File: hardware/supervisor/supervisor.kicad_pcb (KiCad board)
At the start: 2 copper layers, 65 x 56.5 mm, 42 parts, among them IC1 LM2596-3.3, IC10 SIM900, IC2 ULN2003A, IC3 MAX1161?, IC4 ACS723LLCTR-10AU-T, IC5 ACS723LLCTR-10AU-T, IC6 ACS723LLCTR-10AU-T, IC7 ACS723LLCTR-10AU-T, IC8 NLSX4373, IC9 NLSX4373, K1 RELAY, K2 RELAY, P1 RASPI-CONNECT, P2 POWER, P3 RELAY CONNECTOR, P4 TO STRINGS, P5 TO GAK, SW1 SW_PUSH, SW2 SW_PUSH, U1 RF_CONN, U2 SIM_HOLDER

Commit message: master pcb work
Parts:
- added P6: string2, Pin_Headers:Pin_Header_Straight_2x01, F.Cu at (152.4, 153.7)
- added P7: string3, Pin_Headers:Pin_Header_Straight_2x01, F.Cu at (158.8, 153.7)
- C8, IC1: moved to B.Cu
- P4: value TO STRINGS -> string0; footprint Pin_Headers:Pin_Header_Straight_1x04 -> Pin_Headers:Pin_Header_Straight_2x01
- P5: value TO GAK -> string1; footprint Pin_Headers:Pin_Header_Straight_1x04 -> Pin_Headers:Pin_Header_Straight_2x01
- moved IC8 19.1 mm to (134.6, 123.2)
- moved IC9 17.7 mm to (142.2, 123.8)
- moved IC4 13.0 mm to (141.0, 147.3)
- moved P4 12.8 mm to (139.7, 153.7), turned to 0 degrees
- moved P5 10.2 mm to (146.1, 153.7), turned to 0 degrees
- moved IC3 9.38 mm to (150.5, 137.8)
- moved IC5 6.84 mm to (147.3, 147.3)
- moved IC6 6.84 mm to (153.7, 147.3)
- moved D1 2.84 mm to (158.8, 125.7)
- moved L1 2.54 mm to (149.9, 125.7)
- moved IC7 2.54 mm to (160.0, 147.3)
- moved IC1 1.27 mm to (149.9, 115.6)
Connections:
- P4 pad 1: string_in3 -> string_out0
- P4 pad 2: string_in2 -> string_in0
- P5 pad 1: string_out0 -> string_out1
- P5 pad 2: string_out1 -> string_in1
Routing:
- net +5V: track 0.00 -> 31.7 mm
- net Net-(IC10-Pad60): track 0.00 -> 14.1 mm
- net string_in0: track 1.27 -> 4.44 mm
- net string_out3: track 1.27 -> 4.44 mm
- net string_out2: track 1.27 -> 4.44 mm
- net string_out1: track 1.27 -> 4.44 mm
- net string_out0: track 1.27 -> 4.44 mm
- net string_in3: track 1.27 -> 4.44 mm
- net string_in2: track 1.27 -> 4.44 mm
- net string_in1: track 1.27 -> 4.44 mm

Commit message: updated helper files and generated new pcb
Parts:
- removed the C6 at (138.4, 118.1)
- removed the IC7 at (160.0, 147.3)
- removed the P7 at (158.8, 153.7)
- added C10: C_Small, Capacitors_SMD:C_0603, F.Cu at (134.7, 168.9)
- added C11: 0.1u, Capacitors_SMD:C_0603, F.Cu at (122.0, 171.4)
- added C12: 100n, Capacitors_SMD:C_0603, F.Cu at (105.4, 162.6)
- added C13: 1u, Capacitors_SMD:C_0603, F.Cu at (113.0, 168.3)
- added C14: C_Small, Capacitors_SMD:C_0603, F.Cu at (177.3, 133.3)
- added C15: C_Small, Capacitors_SMD:C_0603, F.Cu at (116.8, 158.1)
- added C16: 100n, Capacitors_SMD:C_0603, F.Cu at (132.5, 177.2)
- added C17: C_Small, Capacitors_SMD:C_0603, F.Cu at (154.9, 167.6)
- added C18: C_Small, Capacitors_SMD:C_0603, F.Cu at (139.7, 161.3)
- added C19: C_Small, Capacitors_SMD:C_0603, F.Cu at (122.7, 163.8)
- added C20: C_Small, Capacitors_SMD:C_0603, F.Cu at (110.5, 185.4)
- added C21: C_Small, Capacitors_SMD:C_0603, F.Cu at (146.2, 167.0)
- added C22: 0.1u, Capacitors_SMD:C_0603, F.Cu at (104.8, 181.6)
- added C23: 100n, Capacitors_SMD:C_0603, F.Cu at (166.4, 189.2)
- added C24: 1u, Capacitors_SMD:C_0603, F.Cu at (127.1, 189.9)
- added C25: C_Small, Capacitors_SMD:C_0603, F.Cu at (138.4, 188.0)
- added C26: C_Small, Capacitors_SMD:C_0603, F.Cu at (168.3, 159.4)
- added C27: 100n, Capacitors_SMD:C_0603, F.Cu at (118.7, 181.6)
- added C28: C_Small, Capacitors_SMD:C_0603, F.Cu at (118.2, 149.9)
- added C29: C_Small, Capacitors_SMD:C_0603, F.Cu at (160.7, 160.0)
- added C30: C_Small, Capacitors_SMD:C_0603, F.Cu at (114.9, 163.2)
- added C31: C_Small, Capacitors_SMD:C_0603, F.Cu at (139.7, 170.8)
- added C32: C_Small, Capacitors_SMD:C_0603, F.Cu at (111.2, 175.9)
- added C33: 0.1u, Capacitors_SMD:C_0603, F.Cu at (140.3, 165.7)
- added C34: 100n, Capacitors_SMD:C_0603, F.Cu at (127.6, 167.6)
- added C35: 1u, Capacitors_SMD:C_0603, F.Cu at (138.4, 175.9)
- added C36: C_Small, Capacitors_SMD:C_0603, F.Cu at (178.4, 148.6)
- added C37: C_Small, Capacitors_SMD:C_0603, F.Cu at (123.8, 130.8)
- added C38: 100n, Capacitors_SMD:C_0603, F.Cu at (177.2, 138.4)
- added C39: C_Small, Capacitors_SMD:C_0603, F.Cu at (126.2, 124.5)
- added C40: C_Small, Capacitors_SMD:C_0603, F.Cu at (113.7, 135.9)
- added C8: C_Small, Capacitors_SMD:C_0603, F.Cu at (149.1, 161.3)
- added C9: C_Small, Capacitors_SMD:C_0603, F.Cu at (146.6, 177.2)
- added JP3.1: R_Small, Resistors_SMD:R_0603, F.Cu at (128.7, 127.0)
- added JP3.10: R_Small, Resistors_SMD:R_0603, F.Cu at (115.0, 127.0)
- added JP3.11: R_Small, Resistors_SMD:R_0603, F.Cu at (122.6, 134.0)
- added JP3.12: R_Small, Resistors_SMD:R_0603, F.Cu at (129.7, 130.2)
- added JP3.2: R_Small, Resistors_SMD:R_0603, F.Cu at (129.5, 132.1)
- added JP3.3: R_Small, Resistors_SMD:R_0603, F.Cu at (143.0, 134.0)
- added JP3.4: R_Small, Resistors_SMD:R_0603, F.Cu at (143.0, 128.9)
- added JP3.5: R_Small, Resistors_SMD:R_0603, F.Cu at (149.9, 149.2)
- added JP3.6: R_Small, Resistors_SMD:R_0603, F.Cu at (142.9, 137.2)
- added JP3.7: R_Small, Resistors_SMD:R_0603, F.Cu at (165.7, 149.2)
- added JP3.8: R_Small, Resistors_SMD:R_0603, F.Cu at (160.7, 141.6)
- added JP3.9: R_Small, Resistors_SMD:R_0603, F.Cu at (113.7, 131.4)
- added P1: CONN_01X02, Pin_Headers:Pin_Header_Straight_2x01, F.Cu at (208.9, 134.0)
- added P5: CONN_01X02, Pin_Headers:Pin_Header_Straight_2x01, F.Cu at (196.2, 160.0)
- added P9: CONN_01X02, Pin_Headers:Pin_Header_Straight_2x01, F.Cu at (152.4, 163.8)
- added R10: 100k, Resistors_SMD:R_0603, F.Cu at (177.2, 143.5)
- added R11: 100k, Resistors_SMD:R_0603, F.Cu at (180.3, 125.7)
- added R12: R_Small, Resistors_SMD:R_0603, F.Cu at (134.6, 173.4)
- added R13: R_Small, Resistors_SMD:R_0603, F.Cu at (158.9, 137.2)
- added R14: R_Small, Resistors_SMD:R_0603, F.Cu at (159.4, 134.6)
- added R15: 10k, Resistors_SMD:R_0603, F.Cu at (149.9, 134.0)
- added R16: R_Small, Resistors_SMD:R_0603, F.Cu at (143.4, 139.7)
- added R17: R_Small, Resistors_SMD:R_0603, F.Cu at (136.0, 177.8)
- added R18: 10k, Resistors_SMD:R_0603, F.Cu at (132.1, 135.9)
- added R19: R_Small, Resistors_SMD:R_0603, F.Cu at (136.5, 135.3)
- added R20: R_Small, Resistors_SMD:R_0603, F.Cu at (139.7, 131.4)
- added R21: 50k, Resistors_SMD:R_0603, F.Cu at (179.1, 158.8)
- added R22: 10k, Resistors_SMD:R_0603, F.Cu at (188.6, 154.3)
- added R23: 100k, Resistors_SMD:R_0603, F.Cu at (190.5, 144.1)
- added R24: 100k, Resistors_SMD:R_0603, F.Cu at (188.6, 149.9)
- added R25: 100k, Resistors_SMD:R_0603, F.Cu at (187.3, 134.0)
- added R26: R_Small, Resistors_SMD:R_0603, F.Cu at (148.0, 171.4)
- added R27: R_Small, Resistors_SMD:R_0603, F.Cu at (135.3, 153.0)
- added R28: R_Small, Resistors_SMD:R_0603, F.Cu at (127.0, 148.0)
- added R29: 10k, Resistors_SMD:R_0603, F.Cu at (111.8, 148.0)
- added R30: R_Small, Resistors_SMD:R_0603, F.Cu at (170.8, 153.7)
- added R31: R_Small, Resistors_SMD:R_0603, F.Cu at (172.1, 135.3)
- added R32: 10k, Resistors_SMD:R_0603, F.Cu at (156.8, 153.0)
- added R33: R_Small, Resistors_SMD:R_0603, F.Cu at (163.2, 153.0)
- added R34: R_Small, Resistors_SMD:R_0603, F.Cu at (164.5, 154.3)
- added R35: 50k, Resistors_SMD:R_0603, F.Cu at (190.5, 159.4)
- added R36: 10k, Resistors_SMD:R_0603, F.Cu at (191.8, 138.4)
- added R37: 100k, Resistors_SMD:R_0603, F.Cu at (201.9, 140.3)
- added R38: 100k, Resistors_SMD:R_0603, F.Cu at (199.4, 148.6)
- added R39: 100k, Resistors_SMD:R_0603, F.Cu at (197.5, 153.7)
- added R40: R_Small, Resistors_SMD:R_0603, F.Cu at (125.7, 182.9)
- added R41: R_Small, Resistors_SMD:R_0603, F.Cu at (139.7, 109.9)
- added R42: R_Small, Resistors_SMD:R_0603, F.Cu at (140.3, 122.6)
- added R43: 10k, Resistors_SMD:R_0603, F.Cu at (124.5, 121.9)
- added R44: R_Small, Resistors_SMD:R_0603, F.Cu at (173.4, 158.8)
- added R45: R_Small, Resistors_SMD:R_0603, F.Cu at (141.0, 186.1)
- added R46: 10k, Resistors_SMD:R_0603, F.Cu at (116.2, 123.2)
- added R47: R_Small, Resistors_SMD:R_0603, F.Cu at (121.9, 137.8)
- added R48: R_Small, Resistors_SMD:R_0603, F.Cu at (157.4, 181.6)
- added R49: 50k, Resistors_SMD:R_0603, F.Cu at (198.8, 134.0)
- added R8: 10k, Resistors_SMD:R_0603, F.Cu at (148.1, 182.2)
- added R9: 100k, Resistors_SMD:R_0603, F.Cu at (177.7, 153.7)
- added RV1: POT, pro4:EVM-1USX30B14, F.Cu at (161.9, 136.5)
- added RV2: POT, pro4:EVM-1USX30B14, F.Cu at (146.7, 127.6)
- added RV3: POT, pro4:EVM-1USX30B14, F.Cu at (128.9, 173.4)
- added RV4: POT, pro4:EVM-1USX30B14, F.Cu at (169.5, 153.7)
- added RV5: POT, pro4:EVM-1USX30B14, F.Cu at (143.1, 122.6)
- added RV6: POT, pro4:EVM-1USX30B14, F.Cu at (158.1, 175.9)
- added U1: SC16IS740IPW, Housings_SSOP:TSSOP-16_4.4x5mm_Pitch0.65mm, F.Cu at (198.8, 114.3)
- added U10: CD74HC4046, Housings_SOIC:SOIC-16_7.5x10.3mm_Pitch1.27mm, F.Cu at (125.9, 150.5)
- added U11: CD74HC4046, Housings_SOIC:SOIC-16_7.5x10.3mm_Pitch1.27mm, F.Cu at (155.1, 151.8)
- added U12: OPA376AIDCK, TO_SOT_Packages_SMD:SC-70-6, F.Cu at (143.5, 189.9)
- added U13: CD74HC4046, Housings_SOIC:SOIC-16_7.5x10.3mm_Pitch1.27mm, F.Cu at (135.7, 123.8)
- added U14: CD74HC4046, Housings_SOIC:SOIC-16_7.5x10.3mm_Pitch1.27mm, F.Cu at (121.5, 132.7)
- added U2: SC16IS740IPW, Housings_SSOP:TSSOP-16_4.4x5mm_Pitch0.65mm, F.Cu at (132.7, 113.7)
- added U3: SC16IS740IPW, Housings_SSOP:TSSOP-16_4.4x5mm_Pitch0.65mm, F.Cu at (142.9, 114.3)
- added U6: OPA376AIDCK, TO_SOT_Packages_SMD:SC-70-6, F.Cu at (192.4, 127.0)
- added U7: CD74HC4046, Housings_SOIC:SOIC-16_7.5x10.3mm_Pitch1.27mm, F.Cu at (150.7, 135.3)
- added U8: CD74HC4046, Housings_SOIC:SOIC-16_7.5x10.3mm_Pitch1.27mm, F.Cu at (134.8, 134.0)
- added U9: OPA376AIDCK, TO_SOT_Packages_SMD:SC-70-6, F.Cu at (196.8, 142.9)
- IC3: value MAX1161? -> MAX11612; footprint Housings_SSOP:QSOP-16_3.9x4.9mm_Pitch0.635mm -> Housings_SSOP:TSSOP-8_4.4x3mm_Pitch0.65mm; moved to F.Cu
- K1, K2: value RELAY -> PRINTRELAY_SERIE_36; footprint Relays_ThroughHole:Relay_SPDT_SingleRow_Standing_FinderType34Point51 -> Relays_ThroughHole:Relay_SANYOU_SRD_Series_Form_C
- L1: value INDUCTOR_SMALL -> INDUCTOR_Small
- moved IC3 40.6 mm to (186.1, 118.1)
- moved K2 37.3 mm to (110.5, 117.5)
- moved K1 12.1 mm to (107.3, 147.3)
- renumbered C7 to C6, C8 to C7, D2 to D1, D3 to D2, D4 to D3, D5 to D4, D1 to D5, IC2 to IC1, IC1 to IC2, IC8 to IC7, IC9 to IC8, IC10 to IC9, P1 to P2, P2 to P3, P3 to P4, P4 to P6, P5 to P7, P6 to P8, U1 to U4, U2 to U5
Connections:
- IC1 pad 11: Net-(IC2-Pad11) -> (no net)
- IC1 pad 12: Net-(IC2-Pad12) -> (no net)
- IC3 pad 1: (no net) -> isense0
- IC3 pad 2: (no net) -> isense1
- IC3 pad 3: (no net) -> isense2
- IC3 pad 5: isense0 -> Net-(IC3-Pad5)
- IC3 pad 6: isense1 -> Net-(IC3-Pad6)
- IC3 pad 7: isense2 -> GND
- IC3 pad 8: isense3 -> +5V
- IC7 pad 2: Net-(IC3-Pad14) -> Net-(IC3-Pad6)
- IC7 pad 3: Net-(IC3-Pad13) -> Net-(IC3-Pad5)
- P2 pad 12: (no net) -> IRQ0
- P2 pad 16: (no net) -> IRQ1
- P2 pad 18: (no net) -> IRQ2
- P2 pad 27: (no net) -> SDA
- P2 pad 28: (no net) -> SCL
- P2 pad 3: SDA -> (no net)
- P2 pad 5: SCL -> (no net)
- P2 pad 7: (no net) -> MUCLK
- P4 pad 1: Net-(K1-Pad14) -> Net-(K1-Pad1)
- P4 pad 2: Net-(K1-Pad11) -> Net-(K1-Pad5)
- P4 pad 3: Net-(K1-Pad12) -> Net-(K1-Pad3)
- P4 pad 4: Net-(K2-Pad14) -> Net-(K2-Pad1)
- P4 pad 5: Net-(K2-Pad11) -> Net-(K2-Pad5)
- P4 pad 6: Net-(K2-Pad12) -> Net-(K2-Pad3)
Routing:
- net Net-(K1-Pad12): track 16.9 -> 0.00 mm
- net Net-(K2-Pad12): track 16.9 -> 0.00 mm
- net Net-(K1-Pad11): track 10.7 -> 0.00 mm
- net Net-(K2-Pad11): track 10.7 -> 0.00 mm
- net (no net): track 0.00 -> 8.89 mm
- net Net-(K1-Pad14): track 8.50 -> 0.00 mm
- net Net-(K2-Pad14): track 8.19 -> 0.00 mm
- net string_in3: track 4.44 -> 0.00 mm
- net string_out3: track 4.44 -> 0.00 mm

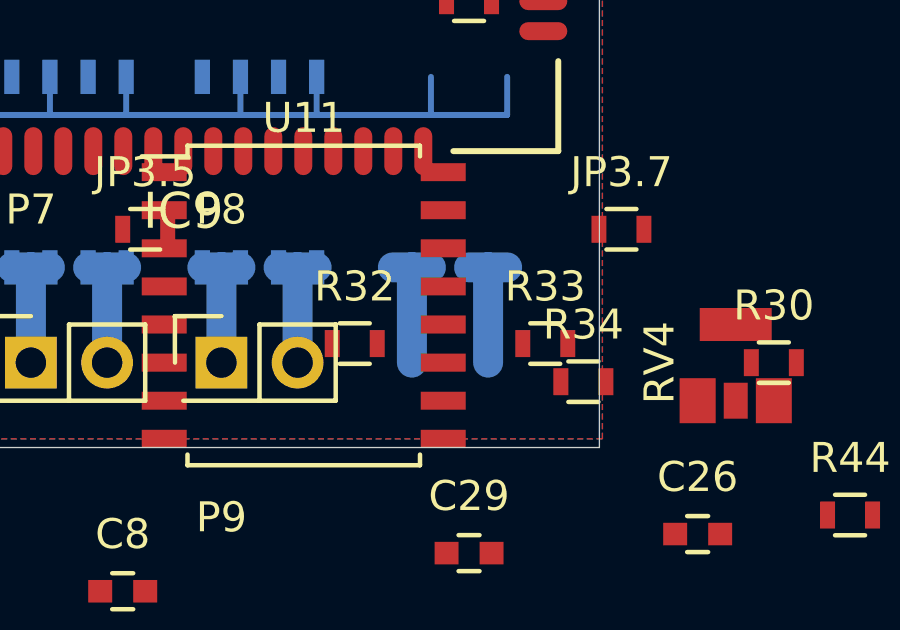
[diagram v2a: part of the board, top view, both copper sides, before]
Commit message: removed dead traces
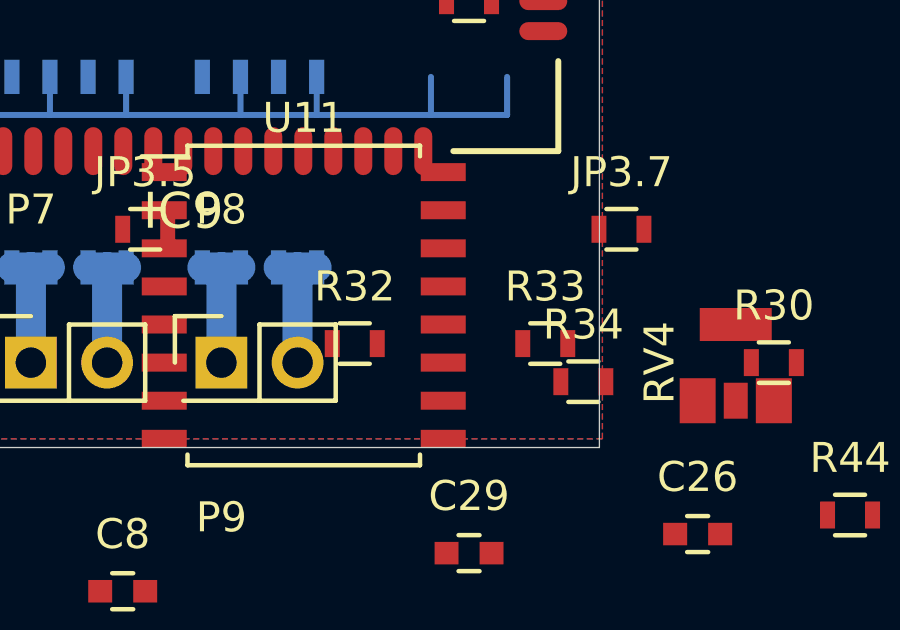
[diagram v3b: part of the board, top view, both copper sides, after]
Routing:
- net (no net): track 8.89 -> 0.00 mm
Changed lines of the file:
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@@
     (thickness 1.6)
     (drawings 4)
-    (tracks 42)
+    (tracks 36)
     (zones 0)
     (modules 149)
@@
   (gr_line (start 165 100) (end 165 156.5) (angle 90) (layer Edge.Cuts) (width 0.001))
   (gr_line (start 100 100) (end 165 100) (angle 90) (layer Edge.Cuts) (width 0.001))
-  (segment (start 158.75 153.67) (end 158.75 150.495) (width 1) (layer B.Cu) (net 0))
-  (segment (start 158.115 150.495) (end 158.75 150.495) (width 1) (layer B.Cu) (net 0))
-  (segment (start 158.75 150.495) (end 159.385 150.495) (width 1) (layer B.Cu) (net 0))
-  (segment (start 161.29 153.67) (end 161.29 150.495) (width 1) (layer B.Cu) (net 0))
-  (segment (start 160.655 150.495) (end 161.29 150.495) (width 1) (layer B.Cu) (net 0))
-  (segment (start 161.29 150.495) (end 161.925 150.495) (width 1) (layer B.Cu) (net 0))
   (segment (start 142.875 145.415) (end 146.685 145.415) (width 0.2) (layer B.Cu) (net 1))
   (segment (start 146.685 144.145) (end 146.685 145.415) (width 0.2) (layer B.Cu) (net 1))
